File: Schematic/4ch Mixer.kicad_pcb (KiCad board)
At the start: 2 copper layers, 30 x 100 mm, 44 parts, among them P1 Power, U1 TL074, U2 TL072

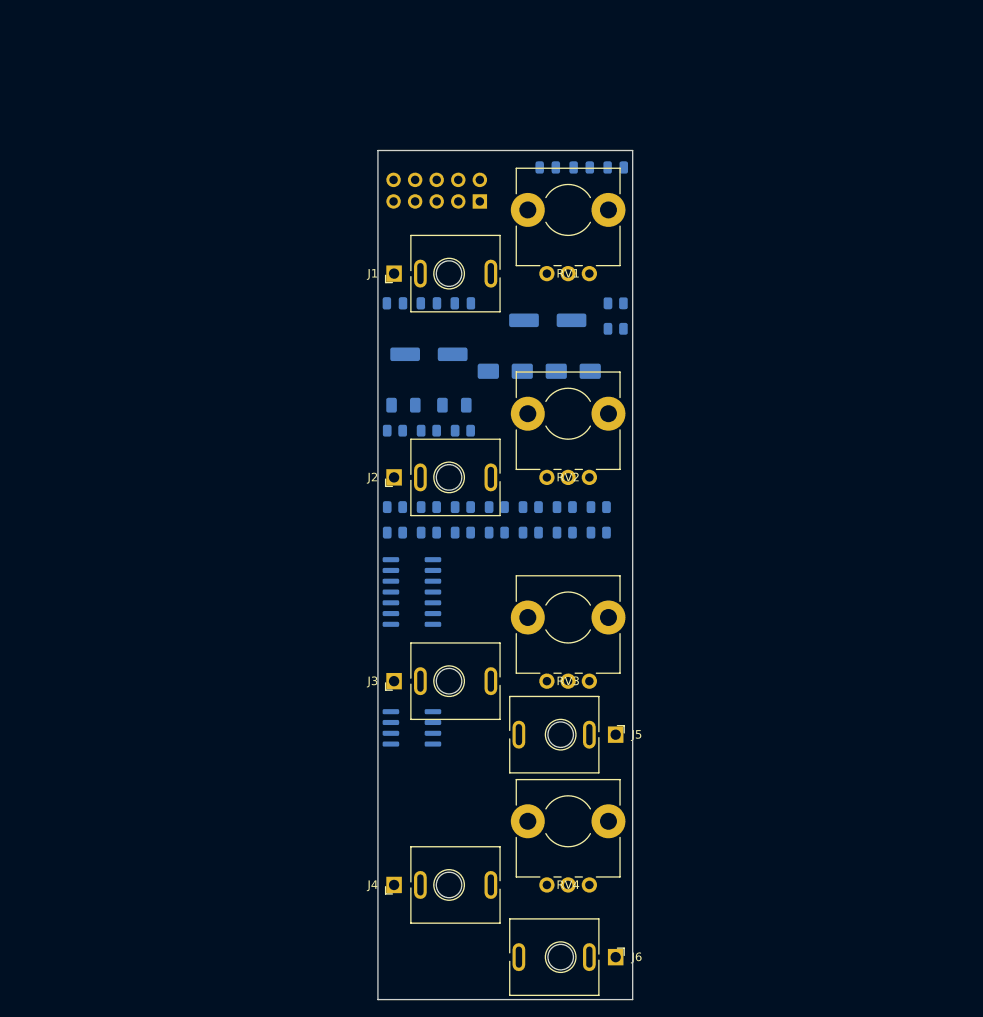
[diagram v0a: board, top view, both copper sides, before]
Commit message: Align pots and input jacks into columns at 24 mm pitch
Pots RV1-RV4 in one column at x=125.5, input jacks J1-J4 in one column at
x=105, both at y = 63, 87, 111, 135. Hand placement otherwise kept. DRC: no
errors.
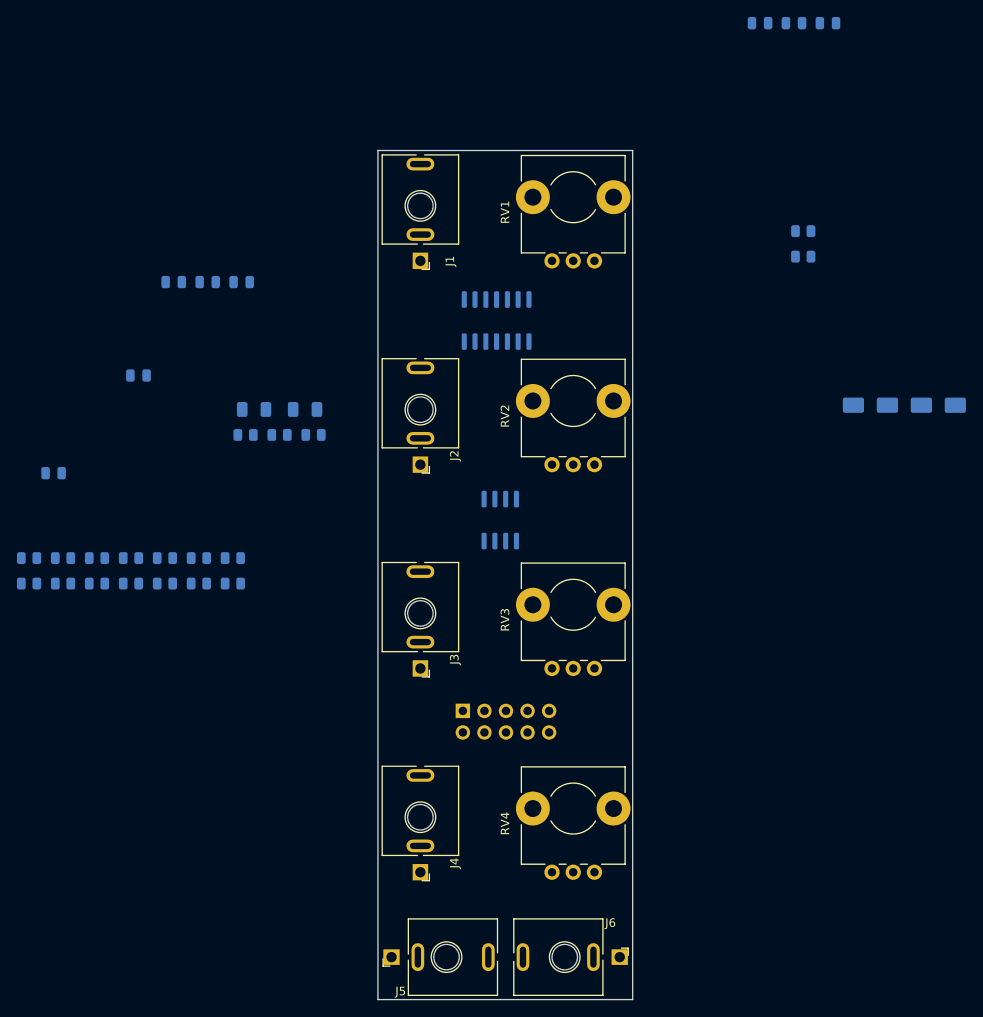
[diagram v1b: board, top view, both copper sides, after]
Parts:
- C1, C2, C3, C4, C7, C8: footprint C_0805_2012Metric -> Capacitor_SMD:C_0805_2012Metric
- C5, C6: value 100uf -> 10uf; footprint CP_Elec_6.3x5.4 -> Capacitor_SMD:C_0805_2012Metric
- D1, D2: footprint D_SMA -> Diode_SMD:D_SMA
- F1, F2: footprint Fuse_1206_3216Metric -> Fuse:Fuse_1206_3216Metric
- J1, J2, J3, J4, J5, J6: footprint Jack_3.5mm_QingPu_WQP-PJ398SM_Vertical_CenterHole_OvalPads -> _NTSFootprints:Jack_3.5mm_QingPu_WQP-PJ398SM_Vertical_CenterHole_OvalPads
- P1: footprint PinHeader_2x05_P2.54mm_Vertical_Shrouded -> _NTSFootprints:PinHeader_2x05_P2.54mm_Vertical_Shrouded
- R1, R10, R11, R12, R13, R14, R15, R16, R17, R18, R19, R2, R3, R4, R5, R6, R7, R8, R9: footprint R_0805_2012Metric -> Resistor_SMD:R_0805_2012Metric
- RV1, RV2, RV3, RV4: footprint Potentiometer_Alps_RK09L_Plated_Mount_Holes -> _NTSFootprints:Potentiometer_Alps_RK09L_Plated_Mount_Holes
- U1: footprint SOIC-14_3.9x8.7mm_P1.27mm -> Package_SO:SOIC-14_3.9x8.7mm_P1.27mm
- U2: footprint SOIC-8_3.9x4.9mm_P1.27mm -> Package_SO:SOIC-8_3.9x4.9mm_P1.27mm
- moved P1 60.0 mm to (110.0, 116.0)
- moved C5 48.6 mm to (71.8, 76.5)
- moved C6 46.4 mm to (61.8, 88.0)
- moved R10 43.5 mm to (74.9, 98.0)
- moved R11 43.5 mm to (78.9, 98.0)
- moved R12 43.5 mm to (82.9, 98.0)
- moved R15 43.5 mm to (66.9, 101.0)
- moved R16 43.5 mm to (70.9, 101.0)
- moved R17 43.5 mm to (74.9, 101.0)
- moved R18 43.5 mm to (78.9, 101.0)
- moved R19 43.5 mm to (82.9, 101.0)
- moved R8 43.5 mm to (66.9, 98.0)
- moved R9 43.5 mm to (70.9, 98.0)
- moved R13 43.5 mm to (58.9, 101.0)
- moved R14 43.5 mm to (62.9, 101.0)
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
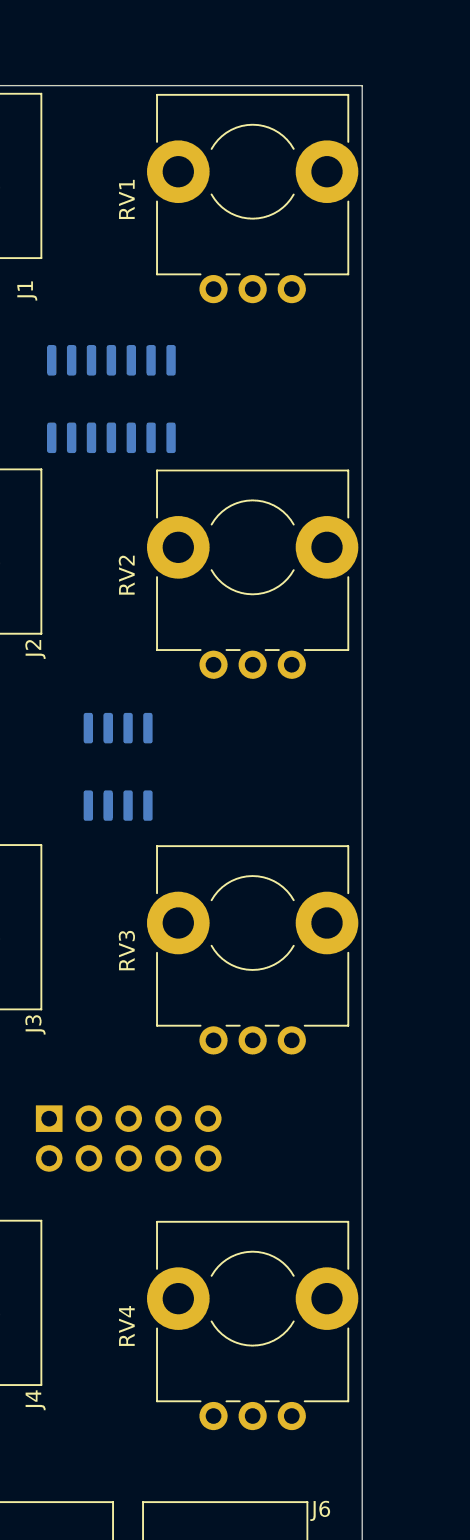
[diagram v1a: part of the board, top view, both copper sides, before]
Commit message: Level pot centres with the input jack centres
Moved RV1-RV4 down 1.02 mm so each pot's graphical circle is on the same
horizontal line as its jack's centre circle.
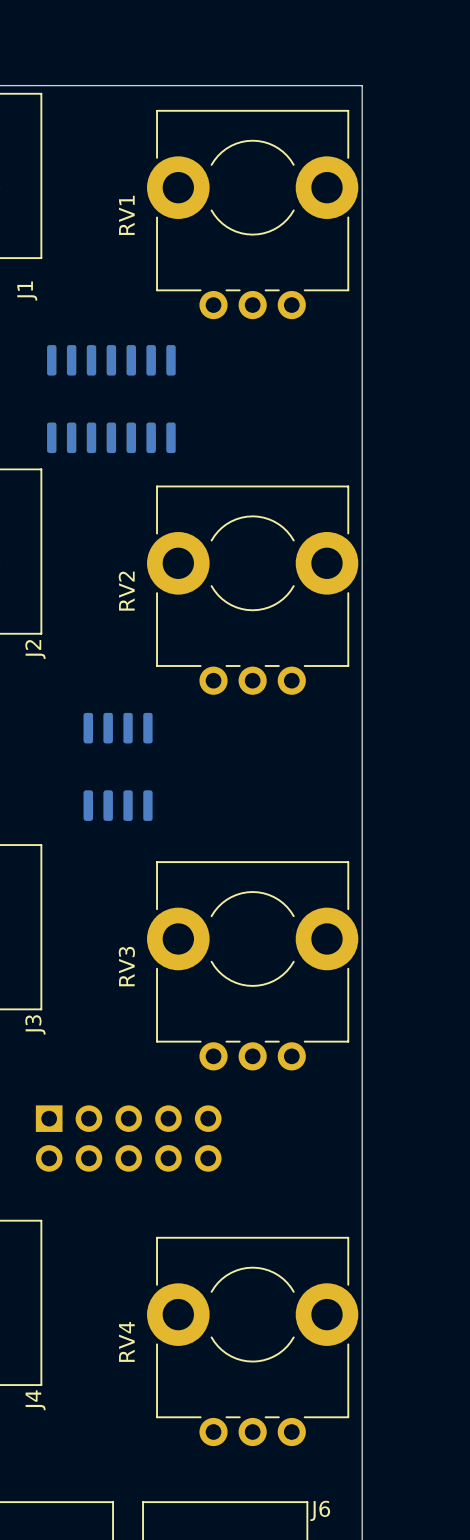
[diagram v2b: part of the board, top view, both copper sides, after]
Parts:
- moved RV4 1.02 mm to (125.5, 136.0)
- moved RV1 1.02 mm to (125.5, 64.0)
- moved RV2 1.02 mm to (125.5, 88.0)
- moved RV3 1.02 mm to (125.5, 112.0)
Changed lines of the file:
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@@
 	(footprint "_NTSFootprints:Potentiometer_Alps_RK09L_Plated_Mount_Holes"
 		(layer "F.Cu")
-		(at 125.5 63.0 90)
+		(at 125.5 64.02 90)
 		(descr "Potentiometer, horizontally mounted, Omeg PC16PU, Omeg PC16PU, Omeg PC16PU, Vishay/Spectrol 248GJ/249GJ Single, Vishay/Spectrol 248GJ/249GJ Single, Vishay/Spectrol 248GJ/249GJ Single, Vishay/Spectrol 248GH/249GH Single, Vishay/Spectrol 148/149 Single, Vishay/Spectrol 148/149 Single, Vishay/Spectrol 148/149 Single, Vishay/Spectrol 148A/149A Single with mounting plates, Vishay/Spectrol 148/149 Double, Vishay/Spectrol 148A/149A Double with mounting plates, Piher PC-16 Single, Piher PC-16 Single, Piher PC-16 Single, Piher PC-16SV Single, Piher PC-16 Double, Piher PC-16 Triple, Piher T16H Single, Piher T16L Single, Piher T16H Double, Alps RK163 Single, Alps RK163 Double, Alps RK097 Single, Alps RK097 Double, Bourns PTV09A-2 Single with mounting sleve Single, Bourns PTV09A-1 with mounting sleve Single, Bourns PRS11S Single, Alps RK09K Single with mounting sleve Single, Alps RK09K with mounting sleve Single, Alps RK09L Single, Alps RK09L Single, http://www.alps.com/prod/info/E/HTML/Potentiometer/RotaryPotentiometers/RK09L/RK09L1140A5E.html")
 		(tags "Potentiometer horizontal  Omeg PC16PU  Omeg PC16PU  Omeg PC16PU  Vishay/Spectrol 248GJ/249GJ Single  Vishay/Spectrol 248GJ/249GJ Single  Vishay/Spectrol 248GJ/249GJ Single  Vishay/Spectrol 248GH/249GH Single  Vishay/Spectrol 148/149 Single  Vishay/Spectrol 148/149 Single  Vishay/Spectrol 148/149 Single  Vishay/Spectrol 148A/149A Single with mounting plates  Vishay/Spectrol 148/149 Double  Vishay/Spectrol 148A/149A Double with mounting plates  Piher PC-16 Single  Piher PC-16 Single  Piher PC-16 Single  Piher PC-16SV Single  Piher PC-16 Double  Piher PC-16 Triple  Piher T16H Single  Piher T16L Single  Piher T16H Double  Alps RK163 Single  Alps RK163 Double  Alps RK097 Single  Alps RK097 Double  Bourns PTV09A-2 Single with mounting sleve Single  Bourns PTV09A-1 with mounting sleve Single  Bourns PRS11S Single  Alps RK09K Single with mounting sleve Single  Alps RK09K with mounting sleve Single  Alps RK09L Single  Alps RK09L Single")
@@
 	(footprint "_NTSFootprints:Potentiometer_Alps_RK09L_Plated_Mount_Holes"
 		(layer "F.Cu")
-		(at 125.5 87.0 90)
+		(at 125.5 88.02 90)
 		(descr "Potentiometer, horizontally mounted, Omeg PC16PU, Omeg PC16PU, Omeg PC16PU, Vishay/Spectrol 248GJ/249GJ Single, Vishay/Spectrol 248GJ/249GJ Single, Vishay/Spectrol 248GJ/249GJ Single, Vishay/Spectrol 248GH/249GH Single, Vishay/Spectrol 148/149 Single, Vishay/Spectrol 148/149 Single, Vishay/Spectrol 148/149 Single, Vishay/Spectrol 148A/149A Single with mounting plates, Vishay/Spectrol 148/149 Double, Vishay/Spectrol 148A/149A Double with mounting plates, Piher PC-16 Single, Piher PC-16 Single, Piher PC-16 Single, Piher PC-16SV Single, Piher PC-16 Double, Piher PC-16 Triple, Piher T16H Single, Piher T16L Single, Piher T16H Double, Alps RK163 Single, Alps RK163 Double, Alps RK097 Single, Alps RK097 Double, Bourns PTV09A-2 Single with mounting sleve Single, Bourns PTV09A-1 with mounting sleve Single, Bourns PRS11S Single, Alps RK09K Single with mounting sleve Single, Alps RK09K with mounting sleve Single, Alps RK09L Single, Alps RK09L Single, http://www.alps.com/prod/info/E/HTML/Potentiometer/RotaryPotentiometers/RK09L/RK09L1140A5E.html")
 		(tags "Potentiometer horizontal  Omeg PC16PU  Omeg PC16PU  Omeg PC16PU  Vishay/Spectrol 248GJ/249GJ Single  Vishay/Spectrol 248GJ/249GJ Single  Vishay/Spectrol 248GJ/249GJ Single  Vishay/Spectrol 248GH/249GH Single  Vishay/Spectrol 148/149 Single  Vishay/Spectrol 148/149 Single  Vishay/Spectrol 148/149 Single  Vishay/Spectrol 148A/149A Single with mounting plates  Vishay/Spectrol 148/149 Double  Vishay/Spectrol 148A/149A Double with mounting plates  Piher PC-16 Single  Piher PC-16 Single  Piher PC-16 Single  Piher PC-16SV Single  Piher PC-16 Double  Piher PC-16 Triple  Piher T16H Single  Piher T16L Single  Piher T16H Double  Alps RK163 Single  Alps RK163 Double  Alps RK097 Single  Alps RK097 Double  Bourns PTV09A-2 Single with mounting sleve Single  Bourns PTV09A-1 with mounting sleve Single  Bourns PRS11S Single  Alps RK09K Single with mounting sleve Single  Alps RK09K with mounting sleve Single  Alps RK09L Single  Alps RK09L Single")
@@
 	(footprint "_NTSFootprints:Potentiometer_Alps_RK09L_Plated_Mount_Holes"
 		(layer "F.Cu")
-		(at 125.5 111.0 90)
+		(at 125.5 112.02 90)
 		(descr "Potentiometer, horizontally mounted, Omeg PC16PU, Omeg PC16PU, Omeg PC16PU, Vishay/Spectrol 248GJ/249GJ Single, Vishay/Spectrol 248GJ/249GJ Single, Vishay/Spectrol 248GJ/249GJ Single, Vishay/Spectrol 248GH/249GH Single, Vishay/Spectrol 148/149 Single, Vishay/Spectrol 148/149 Single, Vishay/Spectrol 148/149 Single, Vishay/Spectrol 148A/149A Single with mounting plates, Vishay/Spectrol 148/149 Double, Vishay/Spectrol 148A/149A Double with mounting plates, Piher PC-16 Single, Piher PC-16 Single, Piher PC-16 Single, Piher PC-16SV Single, Piher PC-16 Double, Piher PC-16 Triple, Piher T16H Single, Piher T16L Single, Piher T16H Double, Alps RK163 Single, Alps RK163 Double, Alps RK097 Single, Alps RK097 Double, Bourns PTV09A-2 Single with mounting sleve Single, Bourns PTV09A-1 with mounting sleve Single, Bourns PRS11S Single, Alps RK09K Single with mounting sleve Single, Alps RK09K with mounting sleve Single, Alps RK09L Single, Alps RK09L Single, http://www.alps.com/prod/info/E/HTML/Potentiometer/RotaryPotentiometers/RK09L/RK09L1140A5E.html")
 		(tags "Potentiometer horizontal  Omeg PC16PU  Omeg PC16PU  Omeg PC16PU  Vishay/Spectrol 248GJ/249GJ Single  Vishay/Spectrol 248GJ/249GJ Single  Vishay/Spectrol 248GJ/249GJ Single  Vishay/Spectrol 248GH/249GH Single  Vishay/Spectrol 148/149 Single  Vishay/Spectrol 148/149 Single  Vishay/Spectrol 148/149 Single  Vishay/Spectrol 148A/149A Single with mounting plates  Vishay/Spectrol 148/149 Double  Vishay/Spectrol 148A/149A Double with mounting plates  Piher PC-16 Single  Piher PC-16 Single  Piher PC-16 Single  Piher PC-16SV Single  Piher PC-16 Double  Piher PC-16 Triple  Piher T16H Single  Piher T16L Single  Piher T16H Double  Alps RK163 Single  Alps RK163 Double  Alps RK097 Single  Alps RK097 Double  Bourns PTV09A-2 Single with mounting sleve Single  Bourns PTV09A-1 with mounting sleve Single  Bourns PRS11S Single  Alps RK09K Single with mounting sleve Single  Alps RK09K with mounting sleve Single  Alps RK09L Single  Alps RK09L Single")
@@
 	(footprint "_NTSFootprints:Potentiometer_Alps_RK09L_Plated_Mount_Holes"
 		(layer "F.Cu")
-		(at 125.5 135.0 90)
+		(at 125.5 136.02 90)
 		(descr "Potentiometer, horizontally mounted, Omeg PC16PU, Omeg PC16PU, Omeg PC16PU, Vishay/Spectrol 248GJ/249GJ Single, Vishay/Spectrol 248GJ/249GJ Single, Vishay/Spectrol 248GJ/249GJ Single, Vishay/Spectrol 248GH/249GH Single, Vishay/Spectrol 148/149 Single, Vishay/Spectrol 148/149 Single, Vishay/Spectrol 148/149 Single, Vishay/Spectrol 148A/149A Single with mounting plates, Vishay/Spectrol 148/149 Double, Vishay/Spectrol 148A/149A Double with mounting plates, Piher PC-16 Single, Piher PC-16 Single, Piher PC-16 Single, Piher PC-16SV Single, Piher PC-16 Double, Piher PC-16 Triple, Piher T16H Single, Piher T16L Single, Piher T16H Double, Alps RK163 Single, Alps RK163 Double, Alps RK097 Single, Alps RK097 Double, Bourns PTV09A-2 Single with mounting sleve Single, Bourns PTV09A-1 with mounting sleve Single, Bourns PRS11S Single, Alps RK09K Single with mounting sleve Single, Alps RK09K with mounting sleve Single, Alps RK09L Single, Alps RK09L Single, http://www.alps.com/prod/info/E/HTML/Potentiometer/RotaryPotentiometers/RK09L/RK09L1140A5E.html")
 		(tags "Potentiometer horizontal  Omeg PC16PU  Omeg PC16PU  Omeg PC16PU  Vishay/Spectrol 248GJ/249GJ Single  Vishay/Spectrol 248GJ/249GJ Single  Vishay/Spectrol 248GJ/249GJ Single  Vishay/Spectrol 248GH/249GH Single  Vishay/Spectrol 148/149 Single  Vishay/Spectrol 148/149 Single  Vishay/Spectrol 148/149 Single  Vishay/Spectrol 148A/149A Single with mounting plates  Vishay/Spectrol 148/149 Double  Vishay/Spectrol 148A/149A Double with mounting plates  Piher PC-16 Single  Piher PC-16 Single  Piher PC-16 Single  Piher PC-16SV Single  Piher PC-16 Double  Piher PC-16 Triple  Piher T16H Single  Piher T16L Single  Piher T16H Double  Alps RK163 Single  Alps RK163 Double  Alps RK097 Single  Alps RK097 Double  Bourns PTV09A-2 Single with mounting sleve Single  Bourns PTV09A-1 with mounting sleve Single  Bourns PRS11S Single  Alps RK09K Single with mounting sleve Single  Alps RK09K with mounting sleve Single  Alps RK09L Single  Alps RK09L Single")

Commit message: Arrange the resistors and capacitors near their connections
place_rest.py places movable parts at the free spot nearest the centroid of
the parts they are wired to, keeping hand-placed parts fixed. Also stop
tracking __pycache__. DRC: no errors.
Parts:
- moved D2 73.9 mm to (114.0, 132.5), turned to 180 degrees
- moved R6 69.3 mm to (121.8, 68.8)
- moved C2 63.6 mm to (122.2, 92.7), turned to 90 degrees
- moved C1 63.2 mm to (119.2, 92.7), turned to 90 degrees
- moved D1 63.1 mm to (123.0, 132.5), turned to 180 degrees
- moved C3 59.9 mm to (101.5, 65.5), turned to 90 degrees
- moved F1 59.5 mm to (123.0, 126.6), turned to -90 degrees
- moved C6 54.6 mm to (111.8, 109.9), turned to 90 degrees
- moved F2 50.9 mm to (113.0, 126.6), turned to -90 degrees
- moved C5 49.8 mm to (108.8, 109.9), turned to 90 degrees
- moved R7 46.0 mm to (101.4, 72.8), turned to 90 degrees
- moved R8 45.4 mm to (104.8, 72.9)
- moved R13 43.4 mm to (101.7, 94.0), turned to 90 degrees
- moved C8 41.2 mm to (101.5, 102.8), turned to 90 degrees
- moved R14 40.0 mm to (101.3, 89.8), turned to 90 degrees
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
